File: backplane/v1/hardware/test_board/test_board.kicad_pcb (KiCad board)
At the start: 2 copper layers, 77 x 77 mm, 1 part, among them J1 Conn_02x20_Odd_Even

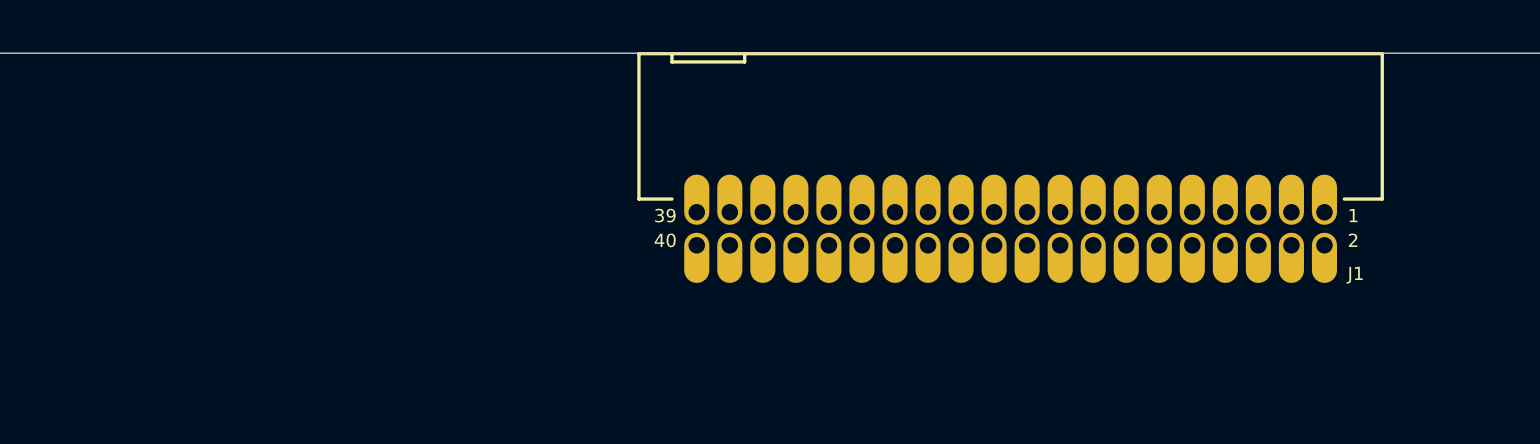
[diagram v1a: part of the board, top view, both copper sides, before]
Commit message: update test board connector placement
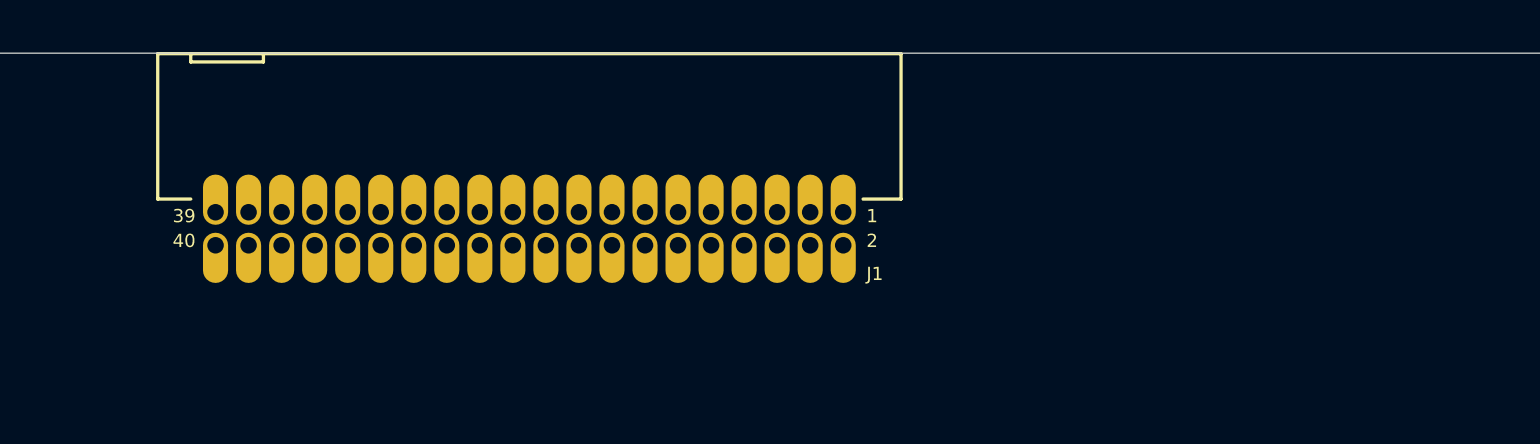
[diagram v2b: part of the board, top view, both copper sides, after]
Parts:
- moved J1 18.5 mm to (127.0, 66.8)
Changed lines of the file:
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@@
 		(locked yes)
 		(layer "F.Cu")
-		(at 145.5 66.75)
+		(at 127 66.75)
 		(property "Reference" "J1"
 			(at 12.954 2.032 0)

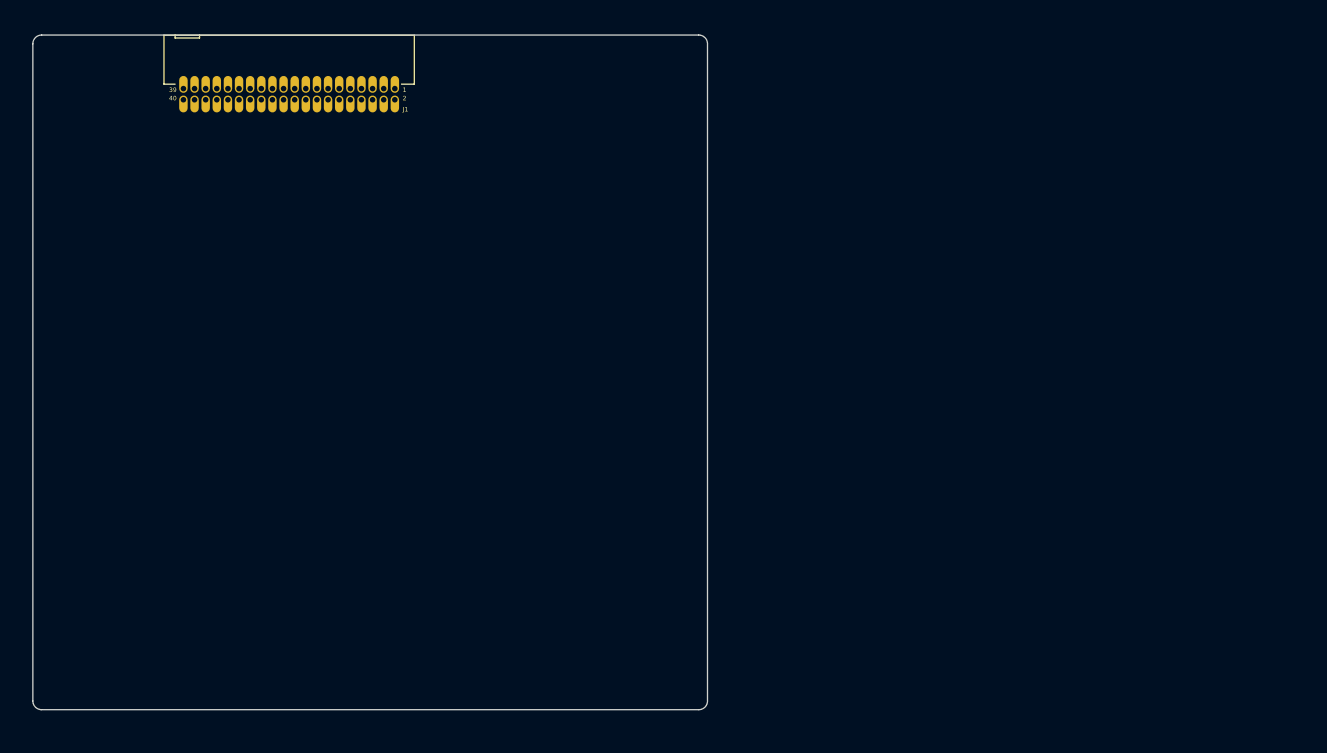
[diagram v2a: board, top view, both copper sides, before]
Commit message: update footprint assignments and start layout
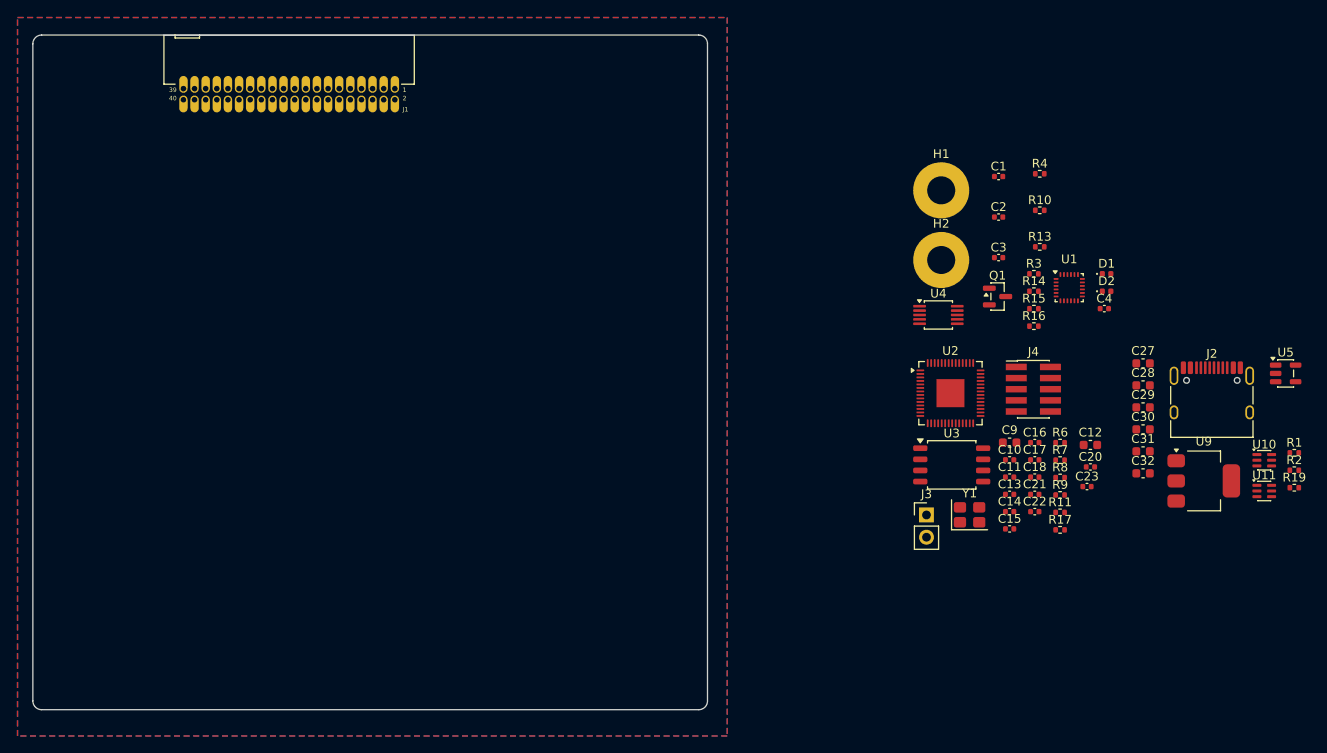
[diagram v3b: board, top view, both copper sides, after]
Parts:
- added C1: 100n, Capacitor_SMD:C_0402_1005Metric, F.Cu at (208.0, 76.2)
- added C10: 100n, Capacitor_SMD:C_0402_1005Metric, F.Cu at (209.2, 108.5)
- added C11: 100n, Capacitor_SMD:C_0402_1005Metric, F.Cu at (209.2, 110.5)
- added C12: 1u, Capacitor_SMD:C_0603_1608Metric, F.Cu at (218.5, 106.8)
- added C13: 100n, Capacitor_SMD:C_0402_1005Metric, F.Cu at (209.2, 112.4)
- added C14: 100n, Capacitor_SMD:C_0402_1005Metric, F.Cu at (209.2, 114.4)
- added C15: 100n, Capacitor_SMD:C_0402_1005Metric, F.Cu at (209.2, 116.4)
- added C16: 100n, Capacitor_SMD:C_0402_1005Metric, F.Cu at (212.1, 106.5)
- added C17: 100n, Capacitor_SMD:C_0402_1005Metric, F.Cu at (212.1, 108.5)
- added C18: 100n, Capacitor_SMD:C_0402_1005Metric, F.Cu at (212.1, 110.5)
- added C2: 100n, Capacitor_SMD:C_0402_1005Metric, F.Cu at (208.0, 80.8)
- added C20: 100n, Capacitor_SMD:C_0402_1005Metric, F.Cu at (218.5, 109.3)
- added C21: 15p, Capacitor_SMD:C_0402_1005Metric, F.Cu at (212.1, 112.4)
- added C22: 15p, Capacitor_SMD:C_0402_1005Metric, F.Cu at (212.1, 114.4)
- added C23: 100n, Capacitor_SMD:C_0402_1005Metric, F.Cu at (218.1, 111.5)
- added C27: 10uF, Capacitor_SMD:C_0603_1608Metric, F.Cu at (224.5, 97.5)
- added C28: 10uF, Capacitor_SMD:C_0603_1608Metric, F.Cu at (224.5, 100.0)
- added C29: 22u, Capacitor_SMD:C_0603_1608Metric, F.Cu at (224.5, 102.5)
- added C3: 100n, Capacitor_SMD:C_0402_1005Metric, F.Cu at (208.0, 85.4)
- added C30: 10uF, Capacitor_SMD:C_0603_1608Metric, F.Cu at (224.5, 105.0)
- added C31: 1uF, Capacitor_SMD:C_0603_1608Metric, F.Cu at (224.5, 107.5)
- added C32: 1uF, Capacitor_SMD:C_0603_1608Metric, F.Cu at (224.5, 110.0)
- added C4: 100n, Capacitor_SMD:C_0402_1005Metric, F.Cu at (220.0, 91.2)
- added C9: 1u, Capacitor_SMD:C_0603_1608Metric, F.Cu at (209.2, 106.5)
- added D1: GREEN, LED_SMD:LED_0402_1005Metric, F.Cu at (220.3, 87.3)
- added D2: RED, LED_SMD:LED_0402_1005Metric, F.Cu at (220.3, 89.2)
- added H1: MountingHole_Pad, MountingHole:MountingHole_3.2mm_M3_Pad, F.Cu at (201.4, 77.7)
- added H2: MountingHole_Pad, MountingHole:MountingHole_3.2mm_M3_Pad, F.Cu at (201.4, 85.7)
- added J2: USB_C_Receptacle_USB2.0_16P, Connector_USB:USB_C_Receptacle_HRO_TYPE-C-31-M-12, F.Cu at (232.3, 102.0)
- added J3: Conn_01x02, Connector_PinHeader_2.54mm:PinHeader_1x02_P2.54mm_Vertical, F.Cu at (199.7, 114.8)
- added J4: Conn_ARM_JTAG_SWD_10, Connector_PinHeader_1.27mm:PinHeader_2x05_P1.27mm_Vertical_SMD, F.Cu at (211.9, 100.4)
- added Q1: Q_NMOS, Package_TO_SOT_SMD:SOT-23, F.Cu at (207.9, 89.8)
- added R1: 5.1k, Resistor_SMD:R_0402_1005Metric, F.Cu at (241.7, 107.7)
- added R10: 150R, Resistor_SMD:R_0402_1005Metric, F.Cu at (212.7, 80.0)
- added R11: DNF, Resistor_SMD:R_0402_1005Metric, F.Cu at (215.0, 114.5)
- added R13: 2m, Resistor_SMD:R_0402_1005Metric, F.Cu at (212.7, 84.2)
- added R14: 10k, Resistor_SMD:R_0402_1005Metric, F.Cu at (212.0, 89.2)
- added R15: 10k, Resistor_SMD:R_0402_1005Metric, F.Cu at (212.0, 91.2)
- added R16: 10k, Resistor_SMD:R_0402_1005Metric, F.Cu at (212.0, 93.2)
- added R17: 10k, Resistor_SMD:R_0402_1005Metric, F.Cu at (215.0, 116.5)
- added R19: 10k, Resistor_SMD:R_0402_1005Metric, F.Cu at (241.7, 111.7)
- added R2: 5.1k, Resistor_SMD:R_0402_1005Metric, F.Cu at (241.7, 109.7)
- added R3: 220R, Resistor_SMD:R_0402_1005Metric, F.Cu at (212.0, 87.3)
- added R4: 150R, Resistor_SMD:R_0402_1005Metric, F.Cu at (212.7, 75.8)
- added R6: 27.4, Resistor_SMD:R_0402_1005Metric, F.Cu at (215.0, 106.5)
- added R7: 27.4, Resistor_SMD:R_0402_1005Metric, F.Cu at (215.0, 108.5)
- added R8: 1k, Resistor_SMD:R_0402_1005Metric, F.Cu at (215.0, 110.5)
- added R9: 1k, Resistor_SMD:R_0402_1005Metric, F.Cu at (215.0, 112.5)
- added U1: ICM-20948, Sensor_Motion:InvenSense_QFN-24_3x3mm_P0.4mm, F.Cu at (216.0, 88.8)
- added U10: LM66100DCK, Package_TO_SOT_SMD:SOT-363_SC-70-6, F.Cu at (238.3, 108.5)
- added U11: LM66100DCK, Package_TO_SOT_SMD:SOT-363_SC-70-6, F.Cu at (238.3, 112.0)
- added U2: RP2040, Package_DFN_QFN:QFN-56-1EP_7x7mm_P0.4mm_EP3.2x3.2mm, F.Cu at (202.5, 100.9)
- added U3: W25Q128JVS, Package_SO:SOIC-8_5.3x5.3mm_P1.27mm, F.Cu at (202.6, 109.1)
- added U4: INA226, Package_SO:TSSOP-10_3x3mm_P0.5mm, F.Cu at (201.1, 92.0)
- added U5: AP2112K-1.8, Package_TO_SOT_SMD:SOT-23-5, F.Cu at (240.7, 98.6)
- added U9: AMS1117-3.3, Package_TO_SOT_SMD:SOT-223-3_TabPin2, F.Cu at (231.4, 110.9)
- added Y1: 12MHz, Crystal:Crystal_SMD_3225-4Pin_3.2x2.5mm, F.Cu at (204.7, 114.8)
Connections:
- net RAIL_1_VOUT renamed /Inter-Board-Connector/RAIL_1_VOUT
- net RAIL_8_VOUT renamed /RAIL_8_VOUT
- J1 pad 21: EPS_PGOOD -> unconnected-(J1-Pin_21-Pad21)
- J1 pad 27: OBC_HEARTBEAT -> unconnected-(J1-Pin_27-Pad27)
- J1 pad 28: EPS_OBC_RESET -> unconnected-(J1-Pin_28-Pad28)
- J1 pad 29: SLOT_ID0 -> unconnected-(J1-Pin_29-Pad29)
- J1 pad 30: OBC_EPS_RESET -> unconnected-(J1-Pin_30-Pad30)
- J1 pad 31: SLOT_ID1 -> unconnected-(J1-Pin_31-Pad31)
- J1 pad 32: SLOT_ID2 -> unconnected-(J1-Pin_32-Pad32)
- J1 pad 33: SPI_SCLK -> unconnected-(J1-Pin_33-Pad33)
- J1 pad 34: SPI_MOSI -> unconnected-(J1-Pin_34-Pad34)
- J1 pad 35: SPI_MISO -> unconnected-(J1-Pin_35-Pad35)
- J1 pad 36: CAN_AUX_P -> unconnected-(J1-Pin_36-Pad36)
- J1 pad 37: SPARE1 -> unconnected-(J1-Pin_37-Pad37)
- J1 pad 38: CAN_AUX_N -> unconnected-(J1-Pin_38-Pad38)
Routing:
- added copper zone on B.Cu, net GND
- added copper zone on F.Cu, net GND
- added copper zone on In1.Cu, net GND
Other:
- copper layers 2 -> 4

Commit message: start layout
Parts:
- added R5: 10k, Resistor_SMD:R_0402_1005Metric, F.Cu at (223.1, 123.8)
- added U6: TCAN3413, Package_SON:VSON-8-1EP_3x3mm_P0.65mm_EP1.65x2.4mm_ThermalVias, F.Cu at (224.7, 120.6)
- C28, C29: footprint Capacitor_SMD:C_0603_1608Metric -> Capacitor_SMD:C_0805_2012Metric
- J1: footprint footprints:J-SAMTEC-TFM-120-X1-XXX-D-RA -> OSUSAT_Connectors:J-SAMTEC-TFM-120-X1-XXX-D-RA
- moved J2 131.7 mm to (101.0, 91.9), turned to -90 degrees
- moved U10 130.5 mm to (111.8, 76.8)
- moved U11 124.9 mm to (117.7, 79.6), turned to -90 degrees
- moved U9 119.9 mm to (114.0, 86.4)
- moved C28 117.0 mm to (108.1, 87.7), turned to 90 degrees
- moved C29 105.6 mm to (120.0, 87.3), turned to -90 degrees
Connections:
- net CAN_MAIN_N renamed /CAN_MAIN_L
- net CAN_MAIN_P renamed /CAN_MAIN_P
- H2 pad 1: Net-(H2-Pad1) -> Net-(Q1-D)
- Q1 pad 1: (no net) -> Net-(Q1-G)
- Q1 pad 2: (no net) -> GND
- Q1 pad 3: (no net) -> Net-(Q1-D)
- R3 pad 2: Net-(Q1-PadG) -> Net-(Q1-G)
- U2 pad 11: unconnected-(U2-GPIO8-Pad11) -> /Peripherals/CAN_TX
- U2 pad 12: unconnected-(U2-GPIO9-Pad12) -> /Peripherals/STB
- U2 pad 9: unconnected-(U2-GPIO7-Pad9) -> /Peripherals/CAN_RX
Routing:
- net GND: track 0.00 -> 1.24 mm, vias 0 -> 6
- added copper zone on In2.Cu, net +3V3
- added copper zone on F.Cu, net Net-(U10-~{CE})

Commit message: replace IMU and continue layout
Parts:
- removed C1, C2, C3: 100n, Capacitor_SMD:C_0402_1005Metric
- removed U1: ICM-20948, Sensor_Motion:InvenSense_QFN-24_3x3mm_P0.4mm
- added C19: 100n, Capacitor_SMD:C_0402_1005Metric, F.Cu at (110.8, 125.8)
- added C24: 220n, Capacitor_SMD:C_0402_1005Metric, F.Cu at (113.4, 122.3)
- added C5: 100n, Capacitor_SMD:C_0402_1005Metric, F.Cu at (110.8, 124.6)
- added C6: 100n, Capacitor_SMD:C_0402_1005Metric, F.Cu at (155.1, 123.6)
- added C7: 100n, Capacitor_SMD:C_0402_1005Metric, F.Cu at (153.0, 120.0)
- added C8: 1u, Capacitor_SMD:C_0603_1608Metric, F.Cu at (110.2, 123.1)
- added R12: 4.7k, Resistor_SMD:R_0402_1005Metric, F.Cu at (122.5, 102.0)
- added R18: 4.7k, Resistor_SMD:R_0402_1005Metric, F.Cu at (123.8, 102.0)
- added U7: LIS2MDL, Package_LGA:LGA-12_2x2mm_P0.5mm, F.Cu at (113.5, 124.3)
- added U8: LSM6DSL, Package_LGA:LGA-14_3x2.5mm_P0.5mm_LayoutBorder3x4y, F.Cu at (152.3, 123.1)
- moved R2 135.2 mm to (107.9, 90.7)
- moved R1 134.6 mm to (107.9, 93.7)
- moved U5 131.1 mm to (109.6, 101.3)
- moved R19 121.9 mm to (123.1, 83.4), turned to -90 degrees
- moved C31 118.1 mm to (106.5, 101.3), turned to -90 degrees
- moved C32 112.0 mm to (112.8, 101.2), turned to -90 degrees
- moved C30 106.1 mm to (121.4, 79.9), turned to 90 degrees
- moved C27 105.9 mm to (120.6, 76.9)
- moved J3 100.5 mm to (100.2, 100.9)
- moved C20 93.3 mm to (127.8, 87.3), turned to 180 degrees
- moved R11 90.1 mm to (126.4, 97.9)
- moved R8 89.8 mm to (126.4, 96.2)
- moved C12 89.6 mm to (129.2, 100.0), turned to 180 degrees
- moved C23 88.6 mm to (129.7, 105.3), turned to 180 degrees
- moved C18 82.9 mm to (129.7, 101.8), turned to 180 degrees
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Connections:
- C12 pad 1: /Inter-Board-Connector/RAIL_1_VOUT -> +3V3
- C13 pad 1: /Inter-Board-Connector/RAIL_1_VOUT -> +3V3
- C14 pad 1: /Inter-Board-Connector/RAIL_1_VOUT -> +3V3
- C15 pad 1: /Inter-Board-Connector/RAIL_1_VOUT -> +3V3
- C16 pad 1: /Inter-Board-Connector/RAIL_1_VOUT -> +3V3
- C17 pad 1: /Inter-Board-Connector/RAIL_1_VOUT -> +3V3
- C18 pad 1: /Inter-Board-Connector/RAIL_1_VOUT -> +3V3
- C23 pad 1: /Inter-Board-Connector/RAIL_1_VOUT -> +3V3
- R14 pad 2: /Peripherals/SDA -> /SHUNT_SDA
- R15 pad 2: /Peripherals/SCL -> /SHUNT_SCL
- U2 pad 1: /Inter-Board-Connector/RAIL_1_VOUT -> +3V3
- U2 pad 10: /Inter-Board-Connector/RAIL_1_VOUT -> +3V3
- U2 pad 12: /Peripherals/STB -> /Peripherals/CAN_RX
- U2 pad 13: unconnected-(U2-GPIO10-Pad13) -> /Peripherals/IMU_INT
- U2 pad 22: /Inter-Board-Connector/RAIL_1_VOUT -> +3V3
- U2 pad 3: /Peripherals/INT -> /Peripherals/SDA
- U2 pad 33: /Inter-Board-Connector/RAIL_1_VOUT -> +3V3
- U2 pad 36: unconnected-(U2-GPIO24-Pad36) -> /SHUNT_SCL
- U2 pad 37: unconnected-(U2-GPIO25-Pad37) -> /SHUNT_SDA
- U2 pad 42: /Inter-Board-Connector/RAIL_1_VOUT -> +3V3
- U2 pad 43: /Inter-Board-Connector/RAIL_1_VOUT -> +3V3
- U2 pad 44: /Inter-Board-Connector/RAIL_1_VOUT -> +3V3
- U2 pad 48: /Inter-Board-Connector/RAIL_1_VOUT -> +3V3
- U2 pad 49: /Inter-Board-Connector/RAIL_1_VOUT -> +3V3
- U2 pad 5: /Peripherals/SDA -> /Peripherals/MNT_INT
- U2 pad 9: /Peripherals/CAN_RX -> /Peripherals/STB
- U4 pad 4: /Peripherals/SDA -> /SHUNT_SDA
- U4 pad 5: /Peripherals/SCL -> /SHUNT_SCL
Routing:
- net +1V8: track 0.00 -> 103.0 mm, vias 0 -> 5
- net /Peripherals/SDA: track 0.00 -> 68.4 mm, vias 0 -> 2
- net /Peripherals/SCL: track 0.00 -> 67.5 mm, vias 0 -> 2
- net /Peripherals/IMU_INT: track 0.00 -> 53.0 mm, vias 0 -> 2
- net GND: track 1.24 -> 45.6 mm, vias 6 -> 39
- net /Peripherals/MNT_INT: track 0.00 -> 35.1 mm, vias 0 -> 2
- net /RP2040/~{USB_BOOT}: track 0.00 -> 30.7 mm, vias 0 -> 1
- net +3V3: track 0.00 -> 28.7 mm, vias 0 -> 11
- net +1V1: track 0.00 -> 28.1 mm, vias 0 -> 2
- net /RP2040/QSPI_SD3: track 0.00 -> 14.6 mm
- net /RP2040/RESET: track 0.00 -> 14.6 mm
- net /RP2040/QSPI_SCLK: track 0.00 -> 13.4 mm, vias 0 -> 2
- net /Inter-Board-Connector/RAIL_1_VOUT: track 0.00 -> 12.9 mm, vias 0 -> 10
- net /RP2040/QSPI_SD0: track 0.00 -> 12.5 mm, vias 0 -> 2
- net /RP2040/SWCLK: track 0.00 -> 11.1 mm, vias 0 -> 2
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- added copper zone on F.Cu, net +1V8
- added copper zone on F.Cu, net +3V3
- added copper zone on F.Cu, net /Inter-Board-Connector/RAIL_1_VOUT
- added copper zone on In2.Cu, net /Inter-Board-Connector/RAIL_1_VOUT
- added copper zone on F.Cu, net /USB & Power OR/VBUS

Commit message: continue layout
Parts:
- added C1: 100n, Capacitor_SMD:C_0402_1005Metric, F.Cu at (124.5, 76.4)
- added R20: 120R, Resistor_SMD:R_0402_1005Metric, F.Cu at (124.5, 70.7)
- moved R5 114.4 mm to (121.7, 70.9)
- moved U6 110.7 mm to (124.5, 73.6), turned to 90 degrees
- moved H2 40.1 mm to (167.2, 106.6)
- moved H1 39.3 mm to (167.6, 97.8)
- moved U4 39.1 mm to (162.1, 89.2)
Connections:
- net /CAN_MAIN_L renamed /CAN_MAIN_N
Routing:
- net /Peripherals/CAN_RX: track 0.00 -> 38.0 mm, vias 0 -> 2
- net /Peripherals/CAN_TX: track 0.00 -> 37.3 mm, vias 0 -> 2
- net /CAN_MAIN_N: track 0.00 -> 6.95 mm, vias 0 -> 1
- net /CAN_MAIN_P: track 0.00 -> 6.86 mm, vias 0 -> 1
- net +3V3: track 28.7 -> 33.3 mm, vias 11 -> 14
- net /Peripherals/STB: track 0.00 -> 2.28 mm, vias 0 -> 1
- net /Inter-Board-Connector/RAIL_1_VOUT: track 12.9 -> 10.7 mm
- net GND: track 45.6 -> 47.1 mm, vias 39 -> 50
- net /Peripherals/IMU_INT: track 53.0 -> 52.0 mm
